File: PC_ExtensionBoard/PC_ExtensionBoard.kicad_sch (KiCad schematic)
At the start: 2 parts, among them CN1 QT002206-4131-3H, CN2 QT002206-4131-3H

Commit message: update 3d
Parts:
- added CN3: HYC70-HDMIA19-230, DatCao_FootPrint:HDMI-TH_HYC70-HDMIA19-230, symbol DatCao_Symbol:root_0_HYC70-HDMIA19-230_
- added DC1: DC-044A-20A, DatCao_FootPrint:DC-IN-TH_DC-044A-20A, symbol DatCao_Symbol:root_0_DC-044A-20A_
- added RJ1: 936273608, DatCao_FootPrint:RJ45-TH_936273608, symbol DatCao_Symbol:root_0_936273608_
- added USB1: HC-USB3.0-L257-J, DatCao_FootPrint:USB-A-TH_HC-USB3.0-L257-J, symbol DatCao_Symbol:root_0_HC-USB3.0-L257-J_
- added USB2: HC-USB2.0-L195-P, DatCao_FootPrint:USB-TH_73725-0110BLF, symbol DatCao_Symbol:root_0_HC-USB2.0-L195-P_

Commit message: update footprint with 3D
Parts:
- removed CN1, CN2: QT002206-4131-3H, DatCao_FootPrint:CORE_BOARD_220PIN_Female, symbol DatCao_Symbol:220Pin_PC_CoreBoard_Female
- removed CN3: HYC70-HDMIA19-230, DatCao_FootPrint:HDMI-TH_HYC70-HDMIA19-230, symbol DatCao_Symbol:root_0_HYC70-HDMIA19-230_
- removed DC1: DC-044A-20A, DatCao_FootPrint:DC-IN-TH_DC-044A-20A, symbol DatCao_Symbol:root_0_DC-044A-20A_
- removed RJ1: 936273608, DatCao_FootPrint:RJ45-TH_936273608, symbol DatCao_Symbol:root_0_936273608_
- removed USB1: HC-USB3.0-L257-J, DatCao_FootPrint:USB-A-TH_HC-USB3.0-L257-J, symbol DatCao_Symbol:root_0_HC-USB3.0-L257-J_
- removed USB2: HC-USB2.0-L195-P, DatCao_FootPrint:USB-TH_73725-0110BLF, symbol DatCao_Symbol:root_0_HC-USB2.0-L195-P_
- added CN1, CN2: QT002206-4131-3H, ACLAB:CONN-SMD_QT002206-4131-3H, symbol ACLAB_Symbol:root_0_QT002206-4131-3H_
- added DC1: DC-044A-20A, ACLAB:DC-IN-TH_DC-044A-20A, symbol ACLAB_Symbol:root_0_DC-044A-20A_
- added HDMI1: HDMI-019S, ACLAB:HDMI-SMD_HDMI-019S, symbol ACLAB_Symbol:root_0_HDMI-019S_
- added PJ1: PJ-327A, ACLAB:AUDIO-IN-SMD_PJ-327A_C22355751, symbol ACLAB_Symbol:root_0_PJ-327A_
- added RJ1: DS1128-09-S8B8S, ACLAB:RJ45-TH_DS1128-09-S8B8S, symbol ACLAB_Symbol:root_0_DS1128-09-S8B8S_
- added U1: HC-USB3.0-L168-WP, ACLAB:USB-TH_USB3.0-A, symbol ACLAB_Symbol:root_0_HC-USB3.0-L168-WP_
- added U2: 10GHz, ACLAB:SMA-TH_SMA-KWE, symbol ACLAB_Symbol:root_0_SMA-KWE_C20415790_
- added USB1: HC-USB3.0-L175-2X1-P, ACLAB:USB-A-TH_H181-AF2R06-12ALCR, symbol ACLAB_Symbol:root_0_HC-USB3.0-L175-2X1-P_
- added USBC1: TYPE-C-31-M-12, ACLAB:USB-C_SMD-TYPE-C-31-M-12_1, symbol ACLAB_Symbol:root_0_TYPE-C-31-M-12_
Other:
- added sheet USB3.0 (USB3.0.kicad_sch)

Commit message: Update Symbol for Coreboard
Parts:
- removed CN1, CN2: QT002206-4131-3H, ACLAB:CONN-SMD_QT002206-4131-3H, symbol ACLAB_Symbol:root_0_QT002206-4131-3H_
- removed DC1: DC-044A-20A, ACLAB:DC-IN-TH_DC-044A-20A, symbol ACLAB_Symbol:root_0_DC-044A-20A_
- removed HDMI1: HDMI-019S, ACLAB:HDMI-SMD_HDMI-019S, symbol ACLAB_Symbol:root_0_HDMI-019S_
- removed PJ1: PJ-327A, ACLAB:AUDIO-IN-SMD_PJ-327A_C22355751, symbol ACLAB_Symbol:root_0_PJ-327A_
- removed RJ1: DS1128-09-S8B8S, ACLAB:RJ45-TH_DS1128-09-S8B8S, symbol ACLAB_Symbol:root_0_DS1128-09-S8B8S_
- removed U1: HC-USB3.0-L168-WP, ACLAB:USB-TH_USB3.0-A, symbol ACLAB_Symbol:root_0_HC-USB3.0-L168-WP_
- removed U2: 10GHz, ACLAB:SMA-TH_SMA-KWE, symbol ACLAB_Symbol:root_0_SMA-KWE_C20415790_
- removed USB1: HC-USB3.0-L175-2X1-P, ACLAB:USB-A-TH_H181-AF2R06-12ALCR, symbol ACLAB_Symbol:root_0_HC-USB3.0-L175-2X1-P_
- removed USBC1: TYPE-C-31-M-12, ACLAB:USB-C_SMD-TYPE-C-31-M-12_1, symbol ACLAB_Symbol:root_0_TYPE-C-31-M-12_
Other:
- removed sheet USB3.0
- added sheet Ethernet_Wifi (Ethernet.kicad_sch)
- added sheet HDMI (HDMI.kicad_sch)
- added sheet PC_CoreBoard (PC_Coreboard.kicad_sch)
- added sheet Power (Power.kicad_sch)
- added sheet USB_Audio (USB.kicad_sch)

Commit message: update schematic: add pattern
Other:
- sheet USB_Audio renamed USB_Audio_RJ45
- removed sheet Ethernet_Wifi
- added sheet M.2 Key E (M.2 Key E.kicad_sch)
- added sheet M.2 Key M #1 (M.2 Key M #1.kicad_sch)
- added sheet MISC (MISC.kicad_sch)
- sheet PC_CoreBoard ports: added GBE0{GbE}, PCIe_{B1x2}{PCIe}, PCIe_{B1x4}{PCIe}, USB2{USB}, USB3{USB}, USB_0_1_OC#; removed none
- sheet USB_Audio_RJ45 ports: added USBSS_2{USBSS}, USB_0_1_OC#, USB_2{USB}; removed none

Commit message: components placement R1
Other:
- sheet MISC ports: added LED_B, LED_G, LED_R, PCIE_{REF0}{PCIe_{REF}}, PCIE_{REF1}{PCIe_{REF}}, PCIE_{REFIN}{PCIe_{REF}}; removed none
- sheet PC_CoreBoard ports: added PCIE_{REF}{PCIe_{REF}}, USB4{USB}, USB5{USB}, USB6{USB}, USB7{USB}, USB_2_3_OC#; removed none
- sheet Power ports: added I2C{I2C}, PSON, PWR_OK, ~{RESET}; removed none

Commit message: update schematic
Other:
- sheet HDMI ports: added DDI1_HPD, DDI1{DDI}, DDI1{I2C}, ~{PWR_LED}/~{PSON}; removed none
- sheet MISC ports: added GPIOEX0, GPIOEX1, GPIOEX2, GPIOEX3, GPIOEX4, GPIOEX5, GPIOEX6, GPIOEX7, MCU_I2C1{I2C}, MCU_I2C2{I2C}; removed none
- sheet PC_CoreBoard ports: added DDI1_HPD, DDI1{DDI}, DDI1{I2C}, USB_4_5_OC#, USB_6_7_OC#, VCC_12V, ~{GBE0_ACT}, ~{GBE0_LINK_1000}, ~{GBE0_LINK}; removed none

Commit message: re-link symbol
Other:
- sheet USB_Audio_RJ45 renamed USB_RJ45
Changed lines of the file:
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@@
 			(color 0 0 0 0)
 		)
-		(property "Sheetname" "USB_Audio_RJ45"
+		(property "Sheetname" "USB_RJ45"
 			(at 97.79 244.3984 0)
 			(show_name no)

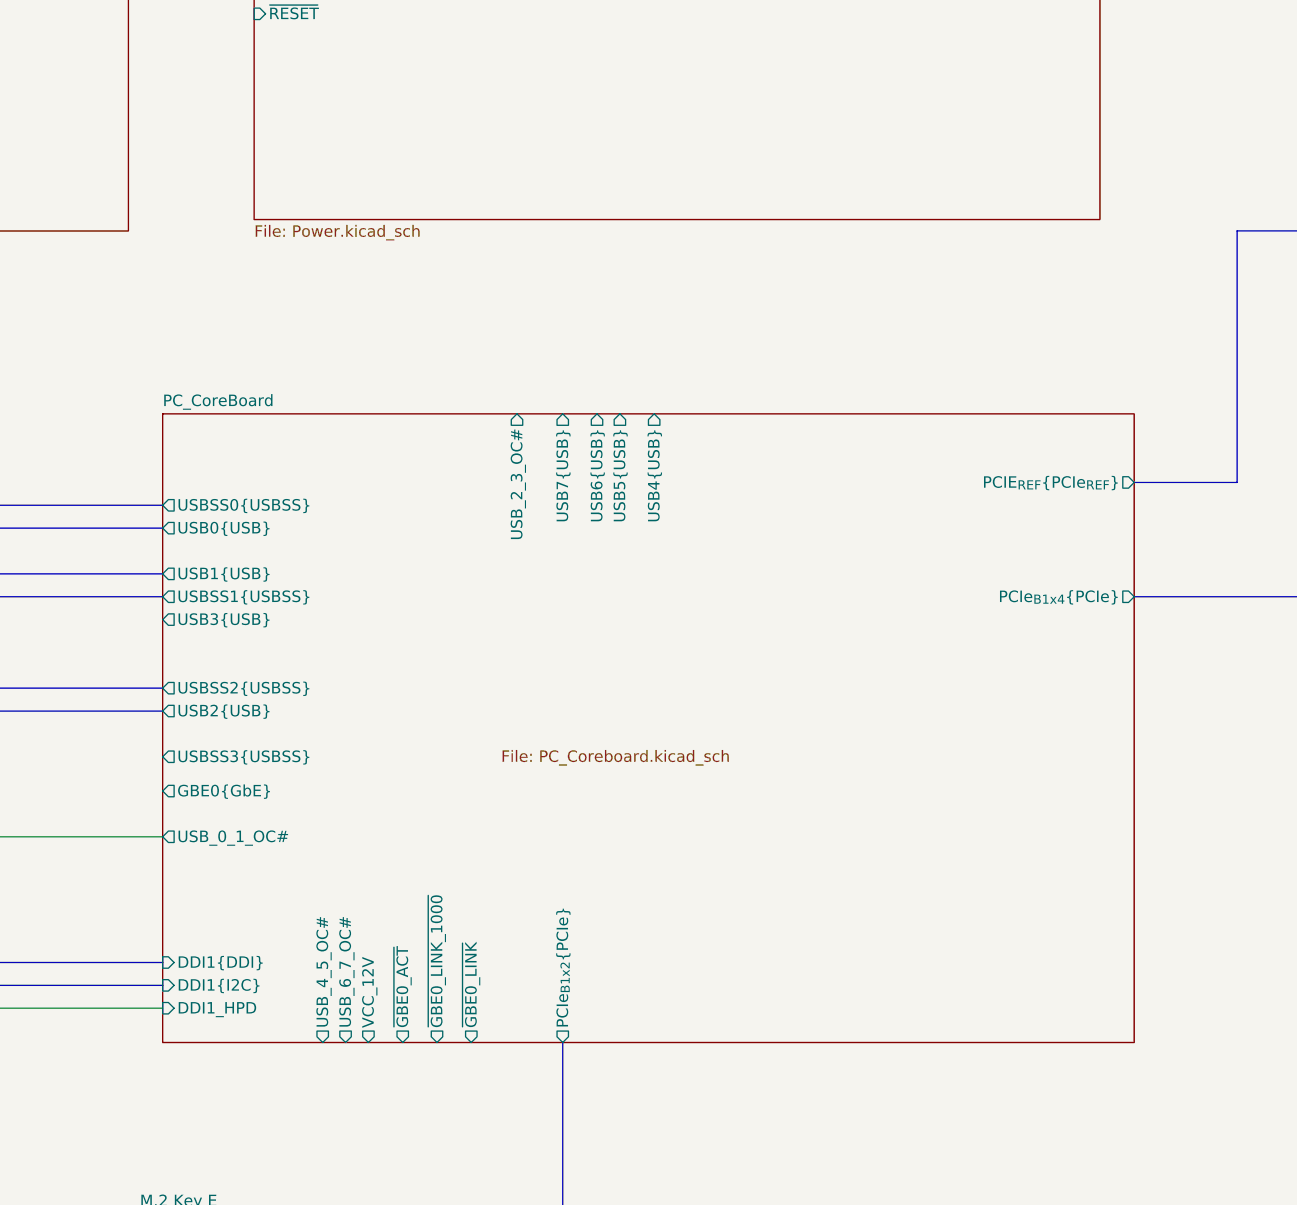
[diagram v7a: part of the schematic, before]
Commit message: update LCSC for HDMI
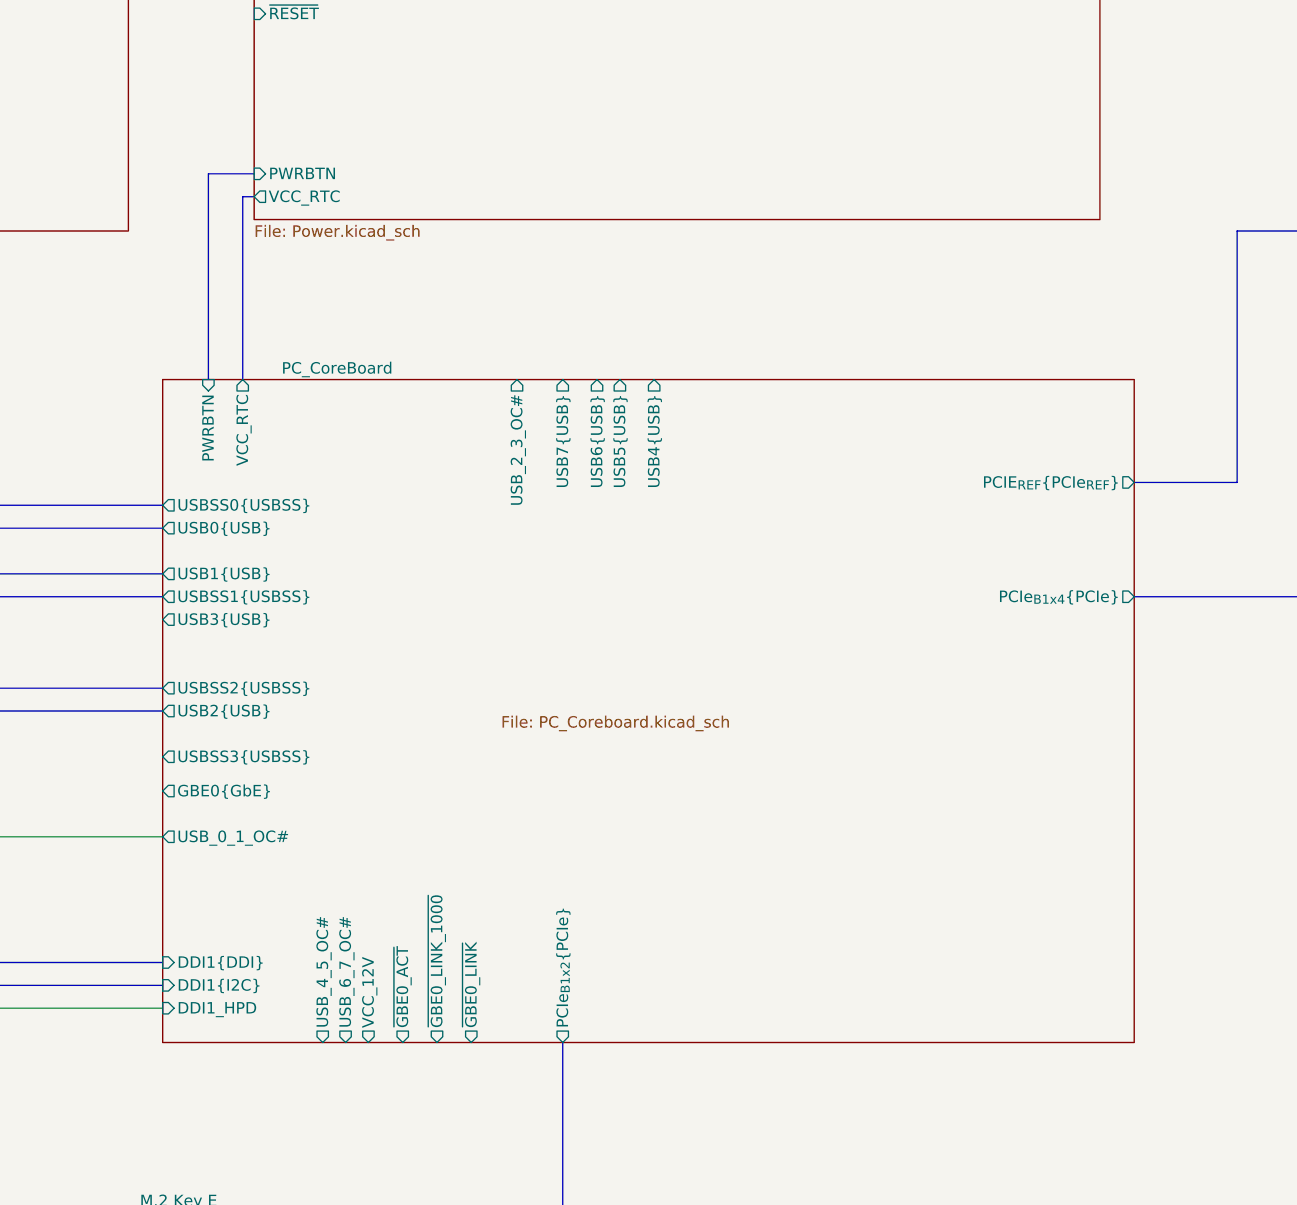
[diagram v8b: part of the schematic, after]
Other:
- sheet PC_CoreBoard ports: added PWRBTN, VCC_RTC; removed none
- sheet Power ports: added PWRBTN, VCC_RTC; removed none
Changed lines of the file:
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@@
+	(bus
+		(pts
+			(xy 209.55 241.3) (xy 209.55 218.44)
+		)
+		(stroke
+			(width 0)
+			(type default)
+		)
+	)
 	(bus
 		(pts
@@
 	(bus
 		(pts
+			(xy 209.55 218.44) (xy 214.63 218.44)
+		)
+		(stroke
+			(width 0)
+			(type default)
+		)
+	)
+	(bus
+		(pts
 			(xy 323.85 224.79) (xy 323.85 252.73)
 		)
@@
 	(bus
 		(pts
+			(xy 213.36 241.3) (xy 213.36 220.98)
+		)
+		(stroke
+			(width 0)
+			(type default)
+		)
+	)
+	(bus
+		(pts
 			(xy 74.93 190.5) (xy 95.25 190.5)
 		)
@@
 		(pts
 			(xy 341.63 224.79) (xy 323.85 224.79)
+		)
+		(stroke
+			(width 0)
+			(type default)
+		)
+	)
+	(bus
+		(pts
+			(xy 213.36 220.98) (xy 214.63 220.98)
 		)
 		(stroke
@@
 	)
 	(sheet
-		(at 204.47 245.11)
-		(size 107.95 69.85)
+		(at 204.47 241.3)
+		(size 107.95 73.66)
 		(exclude_from_sim no)
 		(in_bom yes)
@@
 		)
 		(property "Sheetname" "PC_CoreBoard"
-			(at 204.47 244.3984 0)
+			(at 217.678 240.792 0)
 			(show_name no)
 			(do_not_autoplace no)
@@
 		)
 		(property "Sheetfile" "PC_Coreboard.kicad_sch"
-			(at 242.062 282.448 0)
+			(at 242.062 278.638 0)
 			(show_name no)
 			(do_not_autoplace no)
@@
 		)
 		(pin "USB4{USB}" output
-			(at 259.08 245.11 90)
+			(at 259.08 241.3 90)
 			(effects
 				(font
@@
 		)
 		(pin "USB5{USB}" output
-			(at 255.27 245.11 90)
+			(at 255.27 241.3 90)
 			(effects
 				(font
@@
 		)
 		(pin "USB6{USB}" output
-			(at 252.73 245.11 90)
+			(at 252.73 241.3 90)
 			(effects
 				(font
@@
 		)
 		(pin "USB7{USB}" output
-			(at 248.92 245.11 90)
+			(at 248.92 241.3 90)
 			(effects
 				(font
@@
 		)
 		(pin "USB_2_3_OC#" output
-			(at 243.84 245.11 90)
+			(at 243.84 241.3 90)
 			(effects
 				(font
@@
 				)
 				(justify left)
+			)
+		)
+		(pin "PWRBTN" input
+			(at 209.55 241.3 90)
+			(effects
+				(font
+					(size 1.27 1.27)
+				)
+				(justify right)
+			)
+		)
+		(pin "VCC_RTC" output
+			(at 213.36 241.3 90)
+			(effects
+				(font
+					(size 1.27 1.27)
+				)
+				(justify right)
 			)
 		)
@@
 			)
 		)
+		(pin "PWRBTN" input
+			(at 214.63 218.44 180)
+			(effects
+				(font
+					(size 1.27 1.27)
+				)
+				(justify left)
+			)
+		)
+		(pin "VCC_RTC" output
+			(at 214.63 220.98 180)
+			(effects
+				(font
+					(size 1.27 1.27)
+				)
+				(justify left)
+			)
+		)
